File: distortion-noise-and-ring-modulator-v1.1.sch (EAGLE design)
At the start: 74 parts, among them IC1 TL074JT, IC4 LM13700SL, IC5 TL074JT, Q1 MMBT3906, T1 NOISE-2N3904, U1 MC1496DR2G, X2 MA06-1JN, X3 MA06-1JN

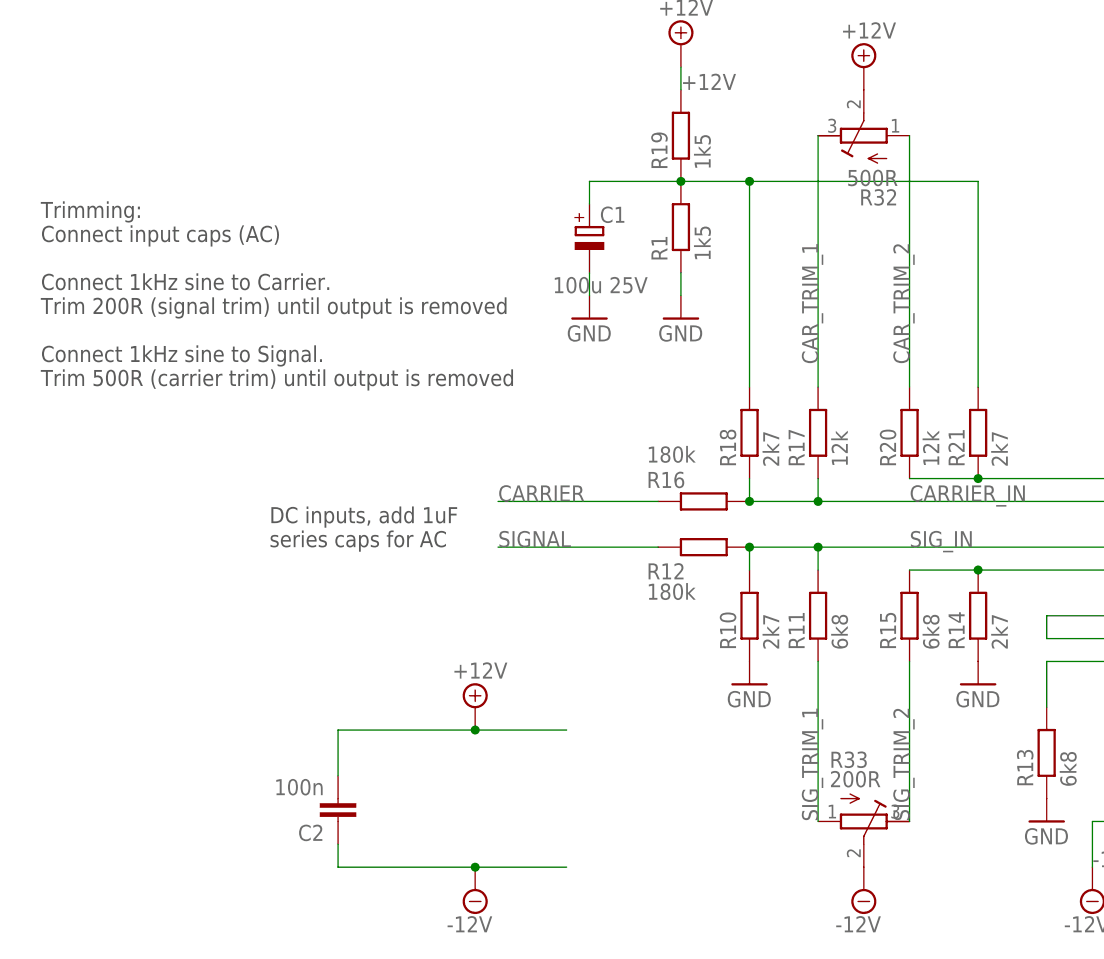
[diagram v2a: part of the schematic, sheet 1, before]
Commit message: Replaced 100uf electrolytic cap with two ceramic. Changed 200R to 500R pot to get a single extended part
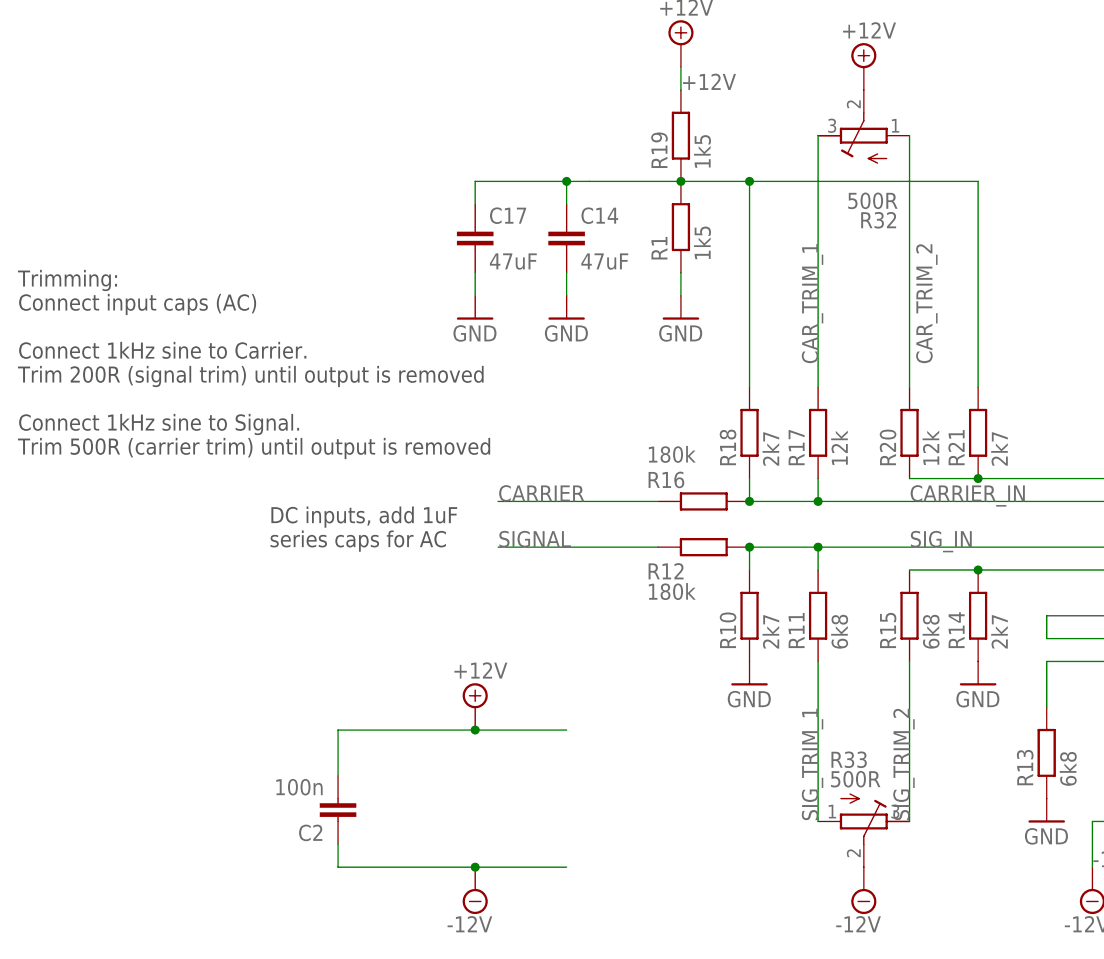
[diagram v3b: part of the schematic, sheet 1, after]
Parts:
- removed C1: 100u 25V, rcl:CPOL-EUE2-5
- added C14, C17: 47uF, rcl:C-EUC1206
- R33: value 200R -> 500R
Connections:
- net GND: now also C14.2, C17.2; no longer C1.-
- net N$9: now also C14.1, C17.1; no longer C1.+
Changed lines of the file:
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@@
 <part name="R1" library="rcl" library_urn="urn:adsk.eagle:library:334" deviceset="R-EU_" device="R0402" package3d_urn="urn:adsk.eagle:package:23547/3" value="1k5"/>
 <part name="R19" library="rcl" library_urn="urn:adsk.eagle:library:334" deviceset="R-EU_" device="R0402" package3d_urn="urn:adsk.eagle:package:23547/3" value="1k5"/>
-<part name="C1" library="rcl" library_urn="urn:adsk.eagle:library:334" deviceset="CPOL-EU" device="E2-5" package3d_urn="urn:adsk.eagle:package:23346/2" value="100u 25V"/>
-<part name="GND3" library="supply1" library_urn="urn:adsk.eagle:library:371" deviceset="GND" device=""/>
 <part name="R13" library="rcl" library_urn="urn:adsk.eagle:library:334" deviceset="R-EU_" device="R0402" package3d_urn="urn:adsk.eagle:package:23547/3" value="6k8"/>
 <part name="GND5" library="supply1" library_urn="urn:adsk.eagle:library:371" deviceset="GND" device=""/>
@@
 <part name="GND24" library="supply1" library_urn="urn:adsk.eagle:library:371" deviceset="GND" device=""/>
 <part name="R32" library="rcl" library_urn="urn:adsk.eagle:library:334" deviceset="R-TRIMM" device="3296X" package3d_urn="urn:adsk.eagle:package:26034/1" value="500R"/>
-<part name="R33" library="rcl" library_urn="urn:adsk.eagle:library:334" deviceset="R-TRIMM" device="3296X" package3d_urn="urn:adsk.eagle:package:26034/1" value="200R"/>
+<part name="R33" library="rcl" library_urn="urn:adsk.eagle:library:334" deviceset="R-TRIMM" device="3296X" package3d_urn="urn:adsk.eagle:package:26034/1" value="500R"/>
 <part name="SUPPLY15" library="supply2" library_urn="urn:adsk.eagle:library:372" deviceset="-12V" device=""/>
 <part name="SUPPLY16" library="supply2" library_urn="urn:adsk.eagle:library:372" deviceset="+12V" device=""/>
 <part name="X2" library="joakim" deviceset="MA06-1J" device="N" value="MA06-1JN"/>
 <part name="X3" library="joakim" deviceset="MA06-1J" device="N" value="MA06-1JN"/>
+<part name="C14" library="rcl" library_urn="urn:adsk.eagle:library:334" deviceset="C-EU" device="C1206" package3d_urn="urn:adsk.eagle:package:23618/2" value="47uF"/>
+<part name="C17" library="rcl" library_urn="urn:adsk.eagle:library:334" deviceset="C-EU" device="C1206" package3d_urn="urn:adsk.eagle:package:23618/2" value="47uF"/>
+<part name="GND25" library="supply1" library_urn="urn:adsk.eagle:library:371" deviceset="GND" device=""/>
+<part name="GND26" library="supply1" library_urn="urn:adsk.eagle:library:371" deviceset="GND" device=""/>
 </parts>
 <sheets>
@@
 <text x="154.94" y="63.5" size="1.778" layer="97">DC output, add a 1uF
 series cap for AC</text>
-<text x="-78.74" y="81.28" size="1.778" layer="97">Trimming:
+<text x="-81.28" y="73.66" size="1.778" layer="97">Trimming:
 Connect input caps (AC)
 Connect 1kHz sine to Carrier.
@@
 <attribute name="VALUE" x="-4.318" y="107.95" size="1.778" layer="96" rot="R90"/>
 </instance>
-<instance part="C1" gate="G$1" x="-17.78" y="101.6" smashed="yes">
-<attribute name="NAME" x="-16.637" y="102.0826" size="1.778" layer="95"/>
-<attribute name="VALUE" x="-11.303" y="96.0374" size="1.778" layer="96" rot="R180"/>
-</instance>
-<instance part="GND3" gate="1" x="-17.78" y="91.44" smashed="yes">
-<attribute name="VALUE" x="-20.32" y="88.9" size="1.778" layer="96"/>
-</instance>
 <instance part="R13" gate="G$1" x="33.02" y="43.18" smashed="yes" rot="R90">
 <attribute name="NAME" x="31.5214" y="39.37" size="1.778" layer="95" rot="R90"/>
@@
 </instance>
 <instance part="R32" gate="G$1" x="12.7" y="111.76" smashed="yes" rot="R90">
-<attribute name="NAME" x="16.51" y="105.791" size="1.778" layer="95" rot="R180"/>
-<attribute name="VALUE" x="16.51" y="107.95" size="1.778" layer="96" rot="R180"/>
+<attribute name="NAME" x="16.51" y="103.251" size="1.778" layer="95" rot="R180"/>
+<attribute name="VALUE" x="16.51" y="105.41" size="1.778" layer="96" rot="R180"/>
 </instance>
 <instance part="R33" gate="G$1" x="12.7" y="35.56" smashed="yes" rot="R270">
@@
 <attribute name="VALUE" x="140.97" y="12.7" size="1.778" layer="96"/>
 <attribute name="NAME" x="140.97" y="33.782" size="1.778" layer="95"/>
+</instance>
+<instance part="C14" gate="G$1" x="-20.32" y="101.6" smashed="yes">
+<attribute name="NAME" x="-18.796" y="101.981" size="1.778" layer="95"/>
+<attribute name="VALUE" x="-18.796" y="96.901" size="1.778" layer="96"/>
+</instance>
+<instance part="C17" gate="G$1" x="-30.48" y="101.6" smashed="yes">
+<attribute name="NAME" x="-28.956" y="101.981" size="1.778" layer="95"/>
+<attribute name="VALUE" x="-28.956" y="96.901" size="1.778" layer="96"/>
+</instance>
+<instance part="GND25" gate="1" x="-20.32" y="91.44" smashed="yes">
+<attribute name="VALUE" x="-22.86" y="88.9" size="1.778" layer="96"/>
+</instance>
+<instance part="GND26" gate="1" x="-30.48" y="91.44" smashed="yes">
+<attribute name="VALUE" x="-33.02" y="88.9" size="1.778" layer="96"/>
 </instance>
 </instances>
@@
 <pinref part="R20" gate="G$1" pin="2"/>
 <wire x1="17.78" y1="83.82" x2="17.78" y2="111.76" width="0.1524" layer="91"/>
-<label x="17.78" y="86.36" size="1.778" layer="95" rot="R90"/>
+<label x="20.32" y="86.36" size="1.778" layer="95" rot="R90"/>
 <pinref part="R32" gate="G$1" pin="A"/>
 </segment>
@@
 </segment>
 <segment>
-<pinref part="C1" gate="G$1" pin="-"/>
-<pinref part="GND3" gate="1" pin="GND"/>
-<wire x1="-17.78" y1="93.98" x2="-17.78" y2="96.52" width="0.1524" layer="91"/>
-</segment>
-<segment>
 <pinref part="R13" gate="G$1" pin="1"/>
 <pinref part="GND5" gate="1" pin="GND"/>
@@
 <wire x1="172.72" y1="25.4" x2="149.86" y2="25.4" width="0.1524" layer="91"/>
 <pinref part="X3" gate="G$1" pin="4"/>
+</segment>
+<segment>
+<pinref part="C14" gate="G$1" pin="2"/>
+<wire x1="-20.32" y1="96.52" x2="-20.32" y2="93.98" width="0.1524" layer="91"/>
+<pinref part="GND25" gate="1" pin="GND"/>
+</segment>
+<segment>
+<pinref part="C17" gate="G$1" pin="2"/>
+<wire x1="-30.48" y1="96.52" x2="-30.48" y2="93.98" width="0.1524" layer="91"/>
+<pinref part="GND26" gate="1" pin="GND"/>
 </segment>
 </net>
@@
 <junction x="0" y="106.68"/>
 <wire x1="-7.62" y1="106.68" x2="-17.78" y2="106.68" width="0.1524" layer="91"/>
-<pinref part="C1" gate="G$1" pin="+"/>
-<wire x1="-17.78" y1="106.68" x2="-17.78" y2="104.14" width="0.1524" layer="91"/>
-</segment>
-</net>
+<wire x1="-17.78" y1="106.68" x2="-20.32" y2="106.68" width="0.1524" layer="91"/>
+<pinref part="C17" gate="G$1" pin="1"/>
+<wire x1="-20.32" y1="106.68" x2="-30.48" y2="106.68" width="0.1524" layer="91"/>
+<wire x1="-30.48" y1="106.68" x2="-30.48" y2="104.14" width="0.1524" layer="91"/>
+<pinref part="C14" gate="G$1" pin="1"/>
+<wire x1="-20.32" y1="104.14" x2="-20.32" y2="106.68" width="0.1524" layer="91"/>
+<junction x="-20.32" y="106.68"/>
+</segment>
+</net>

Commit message: Comments
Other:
- note added: "Yusynth uses a 220R here but tests show that a 500R can be used, the trimming range is just increased."
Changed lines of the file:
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@@
 Trim 500R (carrier trim) until output is removed
 </text>
+<text x="-2.54" y="10.16" size="1.778" layer="91">Yusynth uses a 220R here
+but tests show that a 500R
+can be used, the trimming
+range is just increased.</text>
 </plain>
 <instances>

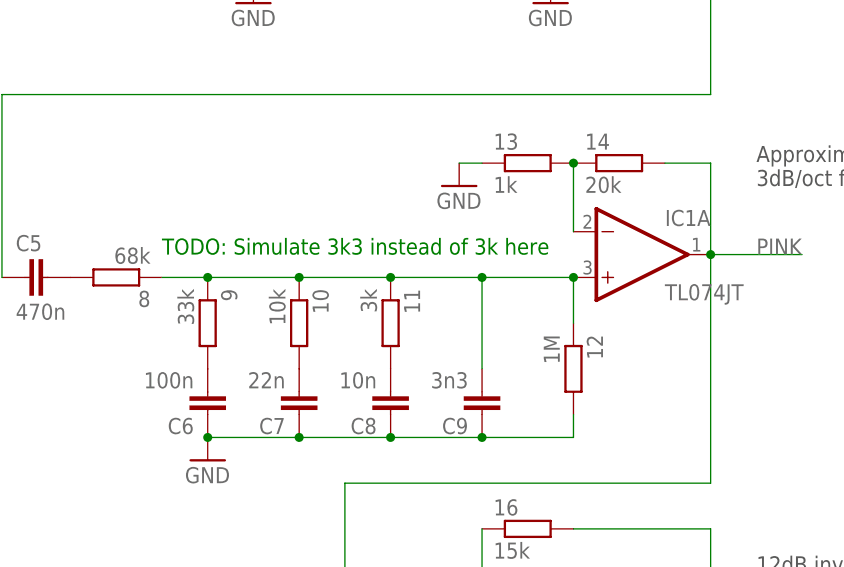
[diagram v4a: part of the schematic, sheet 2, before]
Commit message: Changed to 3k3 on pink filter output to save cost with JLCPCB
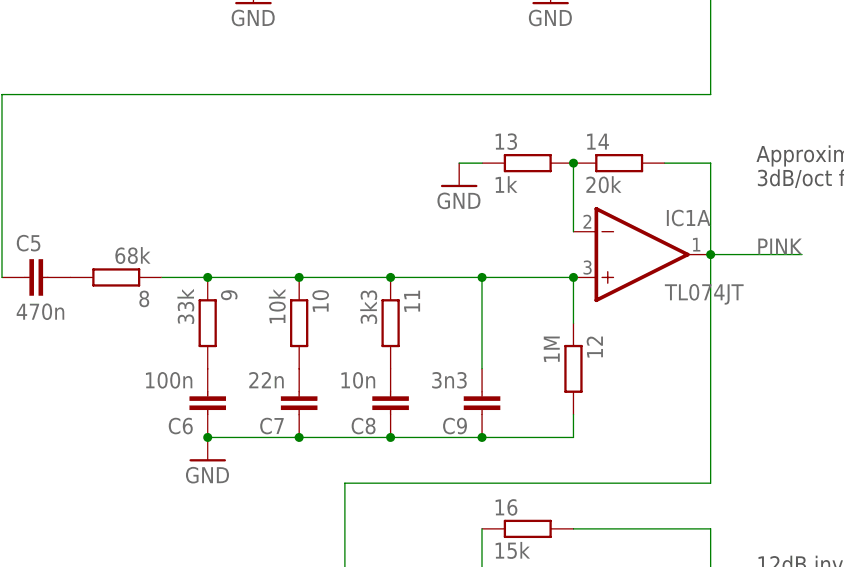
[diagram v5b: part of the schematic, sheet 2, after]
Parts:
- 11: value 3k -> 3k3
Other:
- note removed: "TODO: Simulate 3k3 instead of 3k here"
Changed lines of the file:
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@@
 <part name="9" library="rcl" library_urn="urn:adsk.eagle:library:334" deviceset="R-EU_" device="R0402" package3d_urn="urn:adsk.eagle:package:23547/3" value="33k"/>
 <part name="10" library="rcl" library_urn="urn:adsk.eagle:library:334" deviceset="R-EU_" device="R0402" package3d_urn="urn:adsk.eagle:package:23547/3" value="10k"/>
-<part name="11" library="rcl" library_urn="urn:adsk.eagle:library:334" deviceset="R-EU_" device="R0402" package3d_urn="urn:adsk.eagle:package:23547/3" value="3k"/>
+<part name="11" library="rcl" library_urn="urn:adsk.eagle:library:334" deviceset="R-EU_" device="R0402" package3d_urn="urn:adsk.eagle:package:23547/3" value="3k3"/>
 <part name="12" library="rcl" library_urn="urn:adsk.eagle:library:334" deviceset="R-EU_" device="R0402" package3d_urn="urn:adsk.eagle:package:23547/3" value="1M"/>
 <part name="13" library="rcl" library_urn="urn:adsk.eagle:library:334" deviceset="R-EU_" device="R0402" package3d_urn="urn:adsk.eagle:package:23547/3" value="1k"/>
@@
 not available as
 C0G in 0603 or 0402</text>
-<text x="60.96" y="48.26" size="1.778" layer="91">TODO: Simulate 3k3 instead of 3k here</text>
 </plain>
 <instances>

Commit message: Tested with JLCPCB
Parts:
- removed 1: 220k, rcl:R-EU_R0402
- removed 10: 10k, rcl:R-EU_R0402
- removed 11: 3k3, rcl:R-EU_R0402
- removed 15: 4k7, rcl:R-EU_R0402
- removed 2, 5: 1k, rcl:R-EU_R0402
- removed 4: 100k, rcl:R-EU_R0402
- removed 8: 68k, rcl:R-EU_R0402
- removed 9: 33k, rcl:R-EU_R0402
- removed C17: 47uF, rcl:C-EUC1206
- removed IC5: TL074JT, joakim:TL074JT
- removed X3: MA06-1JN, joakim:MA06-1JN
- added C1: 100n, joakim:C-EU-J0402
- added IC2: TL074JT, joakim:TL074JT
- added R41: 8k2, rcl:R-EU_R0402
- added R42, R46: 33k, rcl:R-EU_R0402
- added R43, R45: 1k, rcl:R-EU_R0402
- added R44: 10k, rcl:R-EU_R0402
- added R47, R49: 510R, rcl:R-EU_R0402
- added R48: 15k, rcl:R-EU_R0402
- added X1: MA06-1JN, joakim:MA06-1JN
- C10: value 220n -> 10n; device joakim:C-EU-J -> joakim:C-EU-J0402
- C11: value 2n2 -> 470n; device joakim:C-EU-J -> joakim:C-EU-J0402
- C12: value 100nF -> 3n3; device joakim:C-EU-J -> joakim:C-EU-J0402
- C13: value 100nF -> 220n; device joakim:C-EU-J -> joakim:C-EU-J0402
- C14: value 47uF -> 2n2; device rcl:C-EUC1206 -> joakim:C-EU-J0402
- C15, C16: device joakim:C-EU-J -> joakim:C-EU-J0402
- C2: value 100n -> 47uF; device joakim:C-EU-J -> rcl:C-EUC1206
- C3: value 470n -> 47uF; device joakim:C-EU-J -> rcl:C-EUC1206
- C4, C5: value 470n -> 100nF; device joakim:C-EU-J -> joakim:C-EU-J0402
- C6: value 100n -> 470n; device joakim:C-EU-J -> joakim:C-EU-J0402
- C7: value 22n -> 470n; device joakim:C-EU-J -> joakim:C-EU-J0402
- C8: value 10n -> 100n; device joakim:C-EU-J -> joakim:C-EU-J0402
- C9: value 3n3 -> 22n; device joakim:C-EU-J -> joakim:C-EU-J0402
- R10: value 2k7 -> 500R; device rcl:R-EU_R0402 -> rcl:R-TRIMM3296X
- R11: value 6k8 -> 12k
- R12: value 180k -> 6k8
- R13: value 6k8 -> 2k7
- R16: value 180k -> 1k2
- R17: value 12k -> 1k2
- R18, R21: value 2k7 -> 15k
- R19: value 1k5 -> 15k
- R2: value 15k -> 1k5
- R20: value 12k -> 15k
- R22: value 200k -> 10k; device pot:TRIM_EU-S64W -> rcl:R-EU_R0402
- R23: value 33k -> 68k
- R24: value 1k -> 220k
- R25: value 1k -> 68k
- R27: value 510R -> 1k
- R28: value 15k -> 100k
- R29: value 510R -> 200k; device rcl:R-EU_R0402 -> rcl:R-TRIMM3296W
- R3: value 68k -> 180k
- R30: value 8k2 -> 10k
- R31: value 10k -> 3k3
- R32: value 500R -> 4k7; device rcl:R-TRIMM3296X -> rcl:R-EU_R0402
- R33: value 500R -> 1k; device rcl:R-TRIMM3296X -> rcl:R-EU_R0402
- R4: value 10k -> 180k
- R5, R6: value 15k -> 2k7
- R7: value 1k2 -> 12k
- R8: value 1k2 -> 6k8
- R9: value 15k -> 500R; device rcl:R-EU_R0402 -> rcl:R-TRIMM3296X
- renumbered 12 to R38, 13 to R34, 14 to R40, 16 to R35, 17 to R36, 6 to R39, 7 to R37, IC4 to IC3
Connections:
- net +12V: now also C1.2, C4.2, IC2P.V+, R1.2, R16.2, R17.1, R24.2, R9.S, X2.6; no longer 1.2, C12.2, C2.2, IC5P.V+, R19.2, R32.S, R7.2, R8.1, X3.6
- net -12V: now also C1.1, C5.1, IC2P.V-, R10.S, X1.1; no longer C13.1, C2.1, IC5P.V-, R33.S, X2.1
- net CARRIER: now also R3.1, X2.3; no longer R16.1, X3.3
- net CARRIER_IN: now also R3.2, R5.1, R7.1; no longer R16.2, R17.1, R18.1
- net CAR_TRIM_1: now also R7.2, R9.E; no longer R17.2, R32.E
- net CAR_TRIM_2: now also R11.2, R9.A; no longer R20.2, R32.A
- net COUT1: now also R17.2, R19.2; no longer R8.2, R9.2
- net COUT2: now also R16.1, R18.2; no longer R6.2, R7.1
- net DIST_CV: now also R41.2, X1.6; no longer R30.2, X2.6
- net DIST_IN: now also R42.1, X1.5; no longer R23.1, X2.5
- net DIST_I_ABC: now also R44.1; no longer R31.1
- net DIST_OUT: now also IC1A.OUT, R46.2, R48.1, X2.1; no longer IC5A.OUT, R26.2, R28.1, X3.1
- net GND: now also C13.1, C2.2, C3.2, C4.1, C5.2, IC1B.+IN, IC2D.+IN, R15.1, R2.1, R20.2, R27.2, R28.2, R33.1, R43.2, R45.1, R47.1, R49.1, R6.1, X2.4; no longer 2.2, 4.2, 5.1, C13.2, C14.2, C17.2, C6.1, C7.1, IC1D.+IN, IC5B.+IN, R1.1, R10.1, R13.1, R2.2, R24.2, R25.1, R27.1, R29.1, X3.4
- net LEV1: now also IC2C.-IN, R27.1, R29.S; no longer 2.1, IC1C.-IN, R22.S
- net LEV2: now also C11.1, IC2C.OUT, R29.A; no longer C4.1, IC1C.OUT, R22.A
- net N$1: now also IC2A.-IN; no longer IC1A.-IN
- net N$10: now also C7.2, IC2C.+IN, R28.1; no longer 4.1, C3.2, IC1C.+IN
- net N$11: now also R15.2; no longer R13.2
- net N$13: now also C11.2, IC2B.+IN; no longer C4.2, IC1B.+IN
- net N$14: now also C12.2, IC2A.+IN, R25.1, R26.1, R30.1, R31.1; no longer 10.1, 11.1, 8.1, 9.1, C9.2, IC1A.+IN
- net N$15: now also IC1C.+IN, R19.1, R20.1; no longer IC5C.+IN, R2.1, R9.1
- net N$16: now also IC1C.-IN, R18.1, R21.1; no longer IC5C.-IN, R5.1, R6.1
- net N$17: now also IC1C.OUT, R21.2, R22.1; no longer IC5C.OUT, R4.1, R5.2
- net N$18: now also IC1B.-IN, R22.2, R23.1; no longer IC5B.-IN, R3.1, R4.2
- net N$19: now also C6.2, R25.2; no longer 8.2, C5.2
- net N$2: now also IC2B.-IN, R33.2; no longer 5.2, IC1B.-IN
- net N$20: now also C13.2, R32.2; no longer 15.2, C10.2
- net N$21: now also C14.2, IC2D.-IN; no longer C11.2, IC1D.-IN
- net N$22: now also IC1D.+IN, R42.2, R43.1; no longer IC5D.+IN, R23.2, R24.1
- net N$23: now also IC1A.+IN, IC1D.-IN, IC1D.OUT; no longer IC5A.+IN, IC5D.-IN, IC5D.OUT
- net N$24: now also IC1A.-IN, R45.2, R46.1; no longer IC5A.-IN, R25.2, R26.1
- net N$25: now also R47.2; no longer R27.2
- net N$26: now also R48.2, R49.2; no longer R28.2, R29.2
- net N$27: now also R41.1; no longer R30.1
- net N$28: now also R44.2; no longer R31.2
- net N$3: now also R12.2; no longer R15.2
- net N$4: now also C8.2, R26.2; no longer 9.2, C6.2
- net N$5: now also C9.2, R30.2; no longer 10.2, C7.2
- net N$6: now also C10.2, R31.2; no longer 11.2, C8.2
- net N$7: now also C7.1, R24.1; no longer 1.1, C3.1
- net N$8: now also R11.1, R13.1; no longer R20.1, R21.1
- net N$9: now also C2.1, C3.1, R1.1, R13.2, R2.2, R5.2; no longer C14.1, C17.1, R1.2, R18.2, R19.1, R21.2
- net OUT: now also IC1B.OUT, R23.2, X2.2; no longer IC5B.OUT, R3.2, X3.2
- net PINK: now also IC2A.OUT, R32.1, X1.2; no longer 15.1, IC1A.OUT, X2.2
- net RED: now also C14.1, IC2D.OUT, X1.3; no longer C11.1, IC1D.OUT, X2.3
- net SIGNAL: now also R4.1, X1.4; no longer R12.1, X2.4
- net SIG_IN: now also R4.2, R6.2, R8.2; no longer R10.2, R11.2, R12.2
- net SIG_TRIM_1: now also R10.A, R8.1; no longer R11.1, R33.A
- net SIG_TRIM_2: now also R10.E, R12.1; no longer R15.1, R33.E
- net WHITE: now also C6.1, IC2B.OUT, X2.5; no longer C5.1, IC1B.OUT, X3.5
